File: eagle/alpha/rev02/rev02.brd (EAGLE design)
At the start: 100 x 80 mm, 386 parts, among them CN1 HOST, CN2 HOST, IC1 N25Q128A13ES, IC2 74AC244DW, IC3 N25Q128A13ES, IC4 74AC244DW, J1 STM32-SWD, Q1 2N7002, Q2 BC818, Q4 2N7002, Q5 ASFL1, Q6 2N7002, T1 BC847, T2 BC847, U1 LMZ13608, U10 ATTINY828R-AU, U12 23K640-I/SN, U13 XC7A200TFBG484, U14 EN6347QI, U15 EN6347QI, U16 EN5364QI, U2 LT3060ITS8-15, U3 MC74HC1G14DTT1G, U4 STM32F429BIT6, U5 IS45S32160F, U6 IS45S32160F, U7 MCP79412-I/SN, U8 FT232H_SERIAL, U9 FT232H_SERIAL, Y1 12 MHz, Y2 12 MHz

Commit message: Maybe final set of review feedback updates.
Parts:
- added C214, C215: 0.1 uF, resistor:C0402
- added FB5, FB6, FB7: 0, UsedComponents:1206
- added IC5, IC6: RCLAMP0502ASC-89, UsedComponents:RCLAMP0502A
- added J2, J3: (no value), SparkFun-Connectors:2X3-NS
- added R83, R84, R85: 0, resistor:R0603
- added R86, R87, R88, R89: 100, resistor:R0402
- R62, R63, R71: device resistor:R1206 -> resistor:R0603
- moved R71 314.4 mm to (-11.4, -175.3)
- moved R62 289.4 mm to (-11.4, -165.1)
- moved R63 282.0 mm to (-11.4, -170.2)
- moved U2 0.57 mm to (11.2, 17.3), turned to 270 degrees
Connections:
- new net FPGA_CFG_CS_N1: R85.2, U13.T19
- new net FPGA_CFG_MISO1: R84.2, U13.R22
- new net FPGA_CFG_MOSI1: R83.2, U13.P22
- new net FPGA_CFG_SCLK1: R71.2, U13.L12
- new net FPGA_INIT_B_INT1: R62.2, U13.U12
- new net FPGA_PROGRAM_B1: R63.2, U13.N12
- new net FT_MGMT_RXD1: R89.2
- new net FT_MGMT_TXD1: R88.2
- new net FT_RXD1: J2.4, J3.4, R87.2, U8.14
- new net FT_TXD1: J2.2, J3.2, R86.2, U8.13
- new net N$57: CN1.D+, IC5.6
- new net N$58: CN1.D-, IC5.4
- new net N$59: CN2.D+, IC6.6
- new net N$60: CN2.D-, IC6.4
- net 15V_LDO_ENABLE: now also U2.1; no longer U2.7
- net 15V_STABLE: now also U2.6; no longer U2.3, U2.4
- net FPGA_CFG_CS_N: now also R85.1; no longer U13.T19
- net FPGA_CFG_MISO: now also R84.1; no longer U13.R22
- net FPGA_CFG_MOSI: now also R83.1; no longer U13.P22
- net FPGA_CFG_SCLK: now also R71.1; no longer U13.L12
- net FPGA_INIT_B_INT: now also R62.1; no longer U13.U12
- net FPGA_PROGRAM_B: now also R63.1; no longer U13.N12
- net FPGA_VCCAUX_1V8: now also FB5.2; no longer R62.2
- net FPGA_VCCINT_1V0: now also FB7.2; no longer R71.2
- net FT_MGMT_RXD: now also R89.1; no longer U9.14
- net FT_MGMT_TXD: now also R88.1; no longer U9.13
- net FT_MGMT_VREGIN: now also IC6.5
- net FT_RXD: now also R87.1; no longer U8.14
- net FT_TXD: now also R86.1; no longer U8.13
- net FT_VREGIN: now also IC5.5
- net GND: now also C214.2, C215.2, IC5.2, IC6.2, J2.6, J3.6, U2.2, U2.3, U2.4; no longer U2.8
- net N$1: now also U2.7; no longer U2.2
- net N$2: now also U2.8; no longer U2.1
- net N$38: now also FB5.1; no longer R62.1
- net N$43: now also FB6.1; no longer R63.1
- net N$48: now also FB7.1; no longer R71.1
- net PWR_18V: no longer U2.6
- net USB_DM: now also IC5.3, J2.3, J3.3; no longer CN1.D-
- net USB_DP: now also IC5.1, J2.5, J3.5; no longer CN1.D+
- net USB_MGMT_DM: now also IC6.3; no longer CN2.D-
- net USB_MGMT_DP: now also IC6.1; no longer CN2.D+
- net VCCO_3V3: now also C214.1, C215.1, FB6.2, J2.1, J3.1; no longer R63.2
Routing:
- net FT_RXD: track 19.9 -> 18.9 mm
- net FT_TXD: track 19.2 -> 18.6 mm

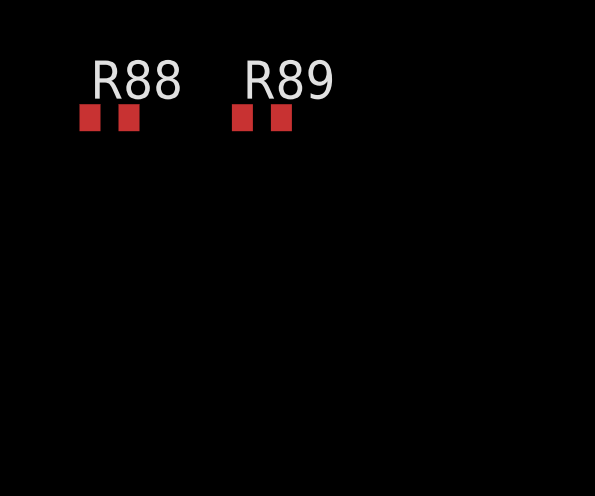
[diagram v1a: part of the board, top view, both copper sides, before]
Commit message: Add FPGA part number and pull-ups to ARM UART RXs
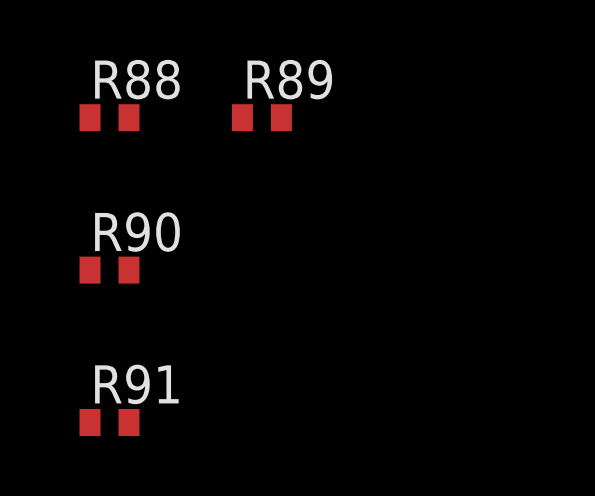
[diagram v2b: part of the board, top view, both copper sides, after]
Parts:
- added R90, R91: 10k, resistor:R0402
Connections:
- net FT_MGMT_TXD: now also R90.2
- net FT_TXD: now also R91.2
- net VCCO_3V3: now also R90.1, R91.1

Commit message: Bugfix copy-paste mistake in USB MGMT UART header.
Also change pinout of header after input from Peter.
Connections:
- net FT_MGMT_RXD1: now also J3.5
- net FT_MGMT_TXD1: now also J3.6
- net FT_RXD1: now also J2.5; no longer J2.4, J3.4
- net FT_TXD1: now also J2.6; no longer J2.2, J3.2
- net GND: now also J2.1, J3.1; no longer J2.6, J3.6
- net USB_DM: no longer J2.3, J3.3
- net USB_DP: no longer J2.5, J3.5
- net USB_MGMT_DM: now also J3.4
- net USB_MGMT_DP: now also J3.3
- net VCCO_3V3: now also J2.2, J3.2; no longer J2.1, J3.1

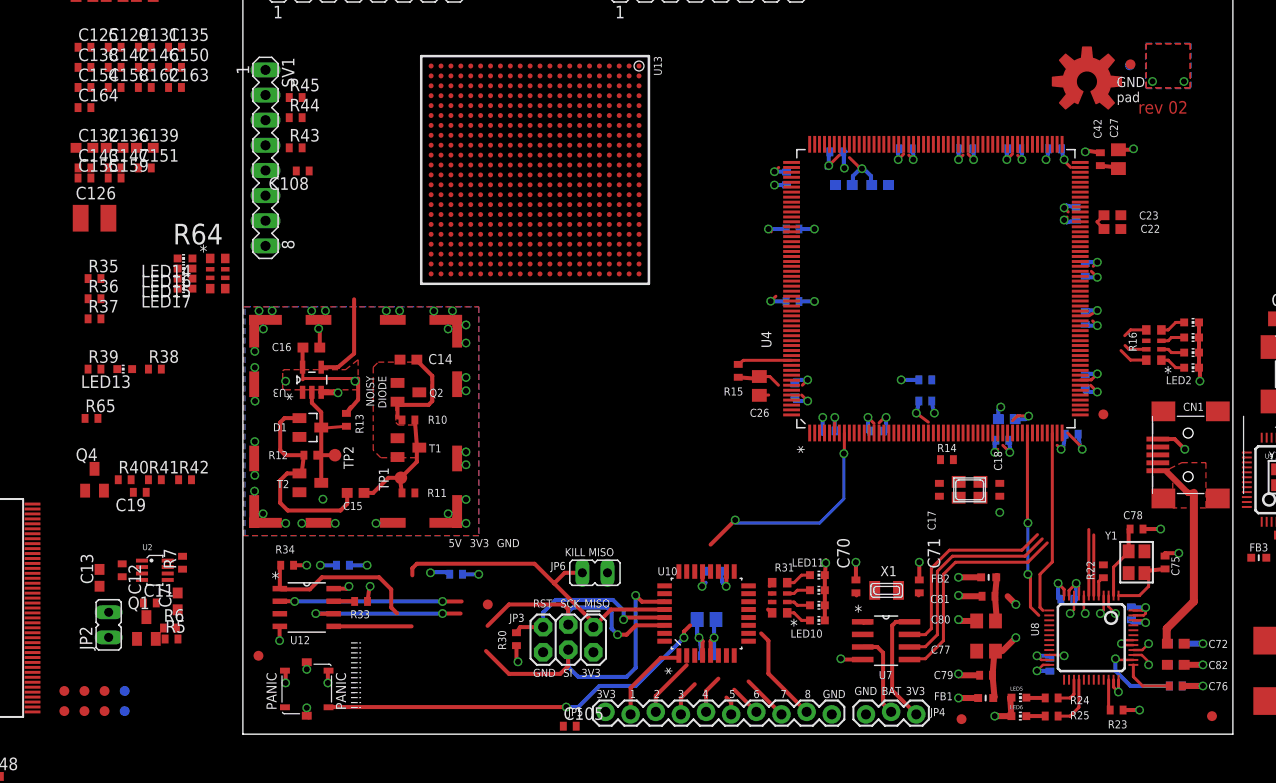
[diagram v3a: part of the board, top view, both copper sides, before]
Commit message: Update text on first page (from Joachim).
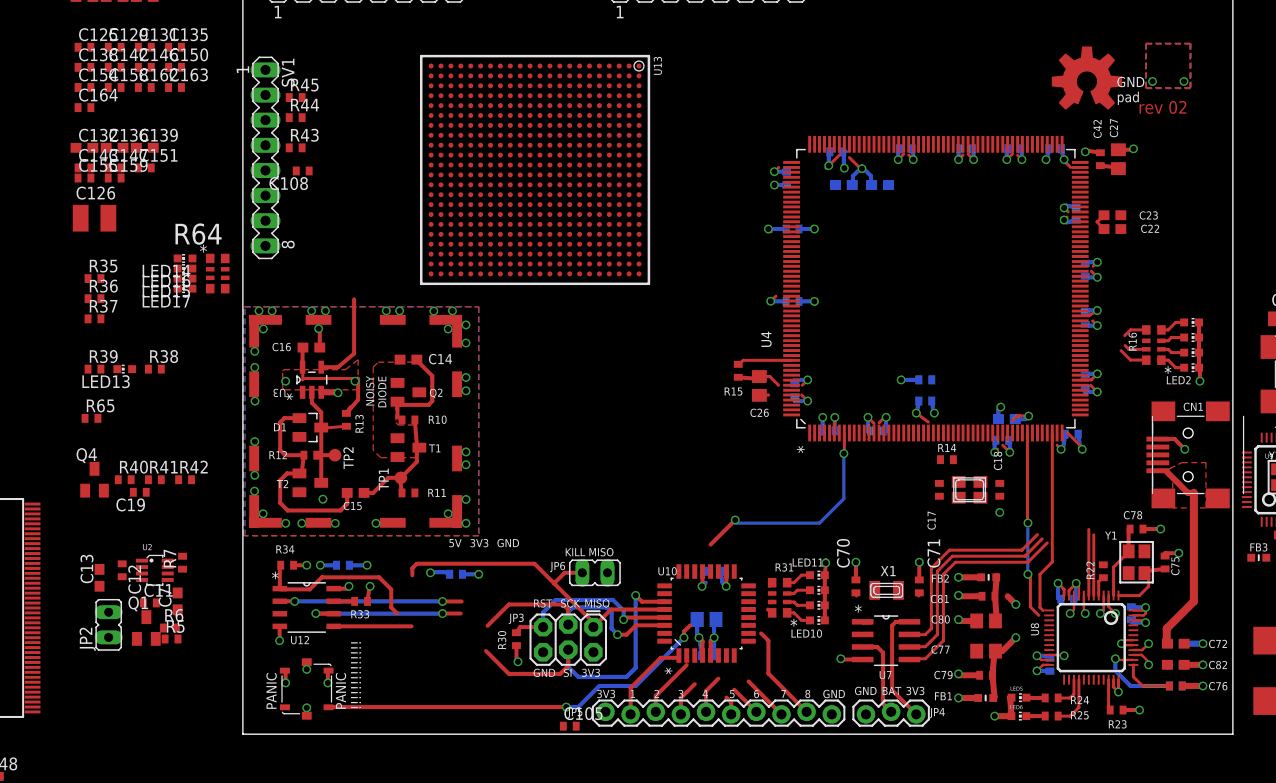
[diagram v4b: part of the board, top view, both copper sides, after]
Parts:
- removed FID1, FID10, FID11, FID12, FID13, FID14, FID15, FID2, FID3, FID4, FID5, FID6, FID7, FID8, FID9: FIDUCIAL1X2, UsedComponents:FIDUCIAL-1X2
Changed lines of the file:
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@@
 <attribute name="NAME" x="24.4514" y="35.5926" size="0.8128" layer="25" font="vector" ratio="10" rot="SR180"/>
 </element>
-<element name="FID9" library="UsedComponents" package="FIDUCIAL-1X2" value="FIDUCIAL1X2" x="6.096" y="5.08" rot="R180"/>
-<element name="FID8" library="UsedComponents" package="FIDUCIAL-1X2" value="FIDUCIAL1X2" x="4.064" y="3.048" rot="R180"/>
-<element name="FID7" library="UsedComponents" package="FIDUCIAL-1X2" value="FIDUCIAL1X2" x="4.064" y="5.08" rot="R180"/>
-<element name="FID10" library="UsedComponents" package="FIDUCIAL-1X2" value="FIDUCIAL1X2" x="8.128" y="5.08" rot="MR180"/>
-<element name="FID11" library="UsedComponents" package="FIDUCIAL-1X2" value="FIDUCIAL1X2" x="8.128" y="3.048" rot="MR180"/>
-<element name="FID12" library="UsedComponents" package="FIDUCIAL-1X2" value="FIDUCIAL1X2" x="109.663" y="68.2824" rot="MR0"/>
 <element name="U4" library="Alpha-IC" package="LQFP-208" value="STM32F429BIT6" x="90.0688" y="45.7176" smashed="yes" rot="R90">
 <attribute name="OC_FARNELL" value="2469581" x="90.0688" y="45.7176" size="1.778" layer="27" rot="R90" display="off"/>
@@
 <attribute name="SUPPLIER" value="ABRACON" x="110.3376" y="18.0848" size="1.778" layer="27" rot="R90" display="off"/>
 </element>
-<element name="FID3" library="UsedComponents" package="FIDUCIAL-1X2" value="FIDUCIAL1X2" x="44.8056" y="13.8176"/>
-<element name="FID2" library="UsedComponents" package="FIDUCIAL-1X2" value="FIDUCIAL1X2" x="2.032" y="3.048" rot="R90"/>
-<element name="FID1" library="UsedComponents" package="FIDUCIAL-1X2" value="FIDUCIAL1X2" x="106.9848" y="33.02"/>
-<element name="FID4" library="UsedComponents" package="FIDUCIAL-1X2" value="FIDUCIAL1X2" x="109.728" y="68.3768"/>
-<element name="FID5" library="UsedComponents" package="FIDUCIAL-1X2" value="FIDUCIAL1X2" x="92.6592" y="2.2352"/>
-<element name="FID6" library="UsedComponents" package="FIDUCIAL-1X2" value="FIDUCIAL1X2" x="6.096" y="3.048" rot="R90"/>
 <element name="U10" library="ATMEL-ATTINY828R-AU" package="QFP80P900X900X120-32N" value="ATTINY828R-AU" x="66.9036" y="12.9032" smashed="yes" rot="R90">
 <attribute name="SUPPLIER" value="ATMEL" x="66.9036" y="12.9032" size="1.778" layer="27" rot="R90" display="off"/>
@@
 <attribute name="RATED_VOLTAGE" value="10V" x="81.9912" y="15.6464" size="1.778" layer="27" rot="R270" display="off"/>
 </element>
-<element name="FID13" library="UsedComponents" package="FIDUCIAL-1X2" value="FIDUCIAL1X2" x="21.6408" y="8.636"/>
-<element name="FID14" library="UsedComponents" package="FIDUCIAL-1X2" value="FIDUCIAL1X2" x="2.032" y="5.08" rot="R90"/>
-<element name="FID15" library="UsedComponents" package="FIDUCIAL-1X2" value="FIDUCIAL1X2" x="117.9576" y="2.54"/>
 <element name="U13" library="Xilinx_XC7A200TFBG484" package="FF484" value="XC7A200TFBG484" x="49.5808" y="57.7088" rot="R270">
 <attribute name="MFR" value="Xilinx" x="49.5808" y="57.7088" size="1.778" layer="27" rot="R270" display="off"/>
